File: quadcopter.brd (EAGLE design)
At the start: 137.3 x 137.3 mm, 69 parts, among them J1 AVR_SPI_PRG_6NS, U1 ATMEGA128RFA1, Y2 16MHz

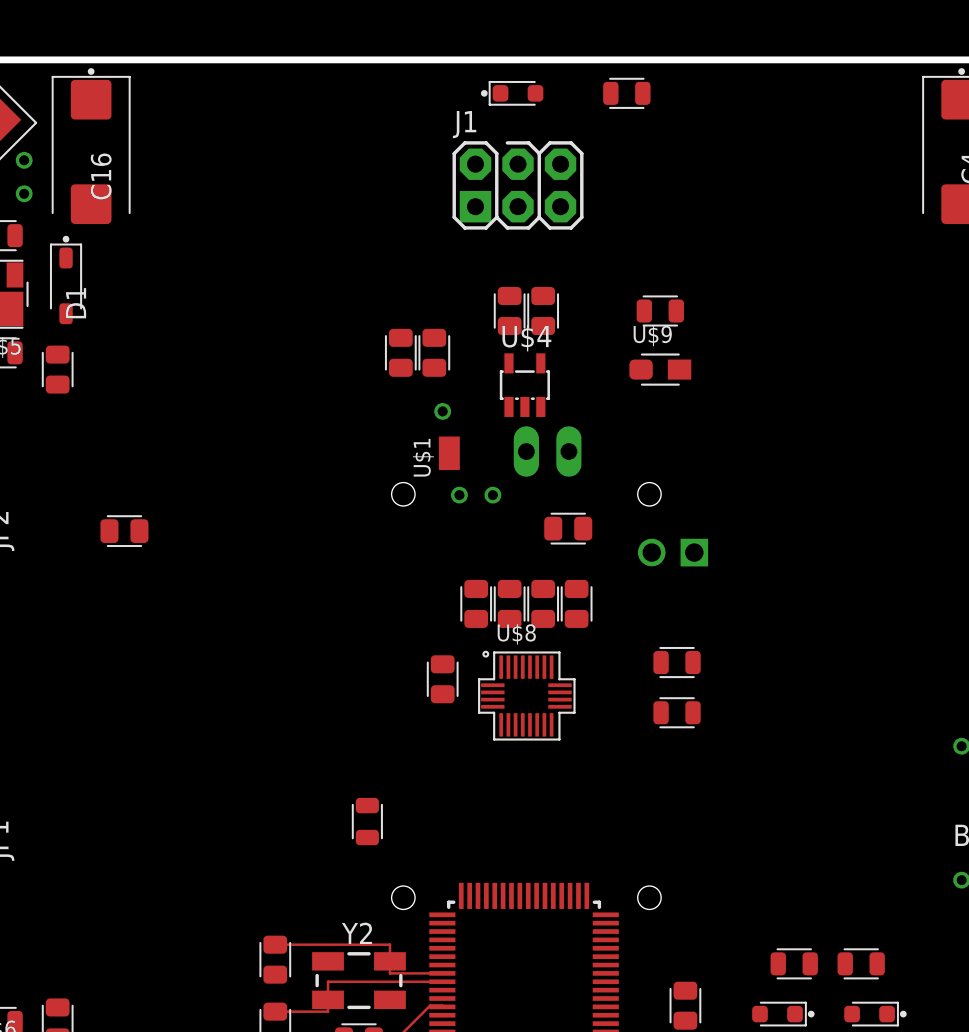
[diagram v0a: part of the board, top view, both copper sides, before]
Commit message: Repositioned battery holder and voltage regulator
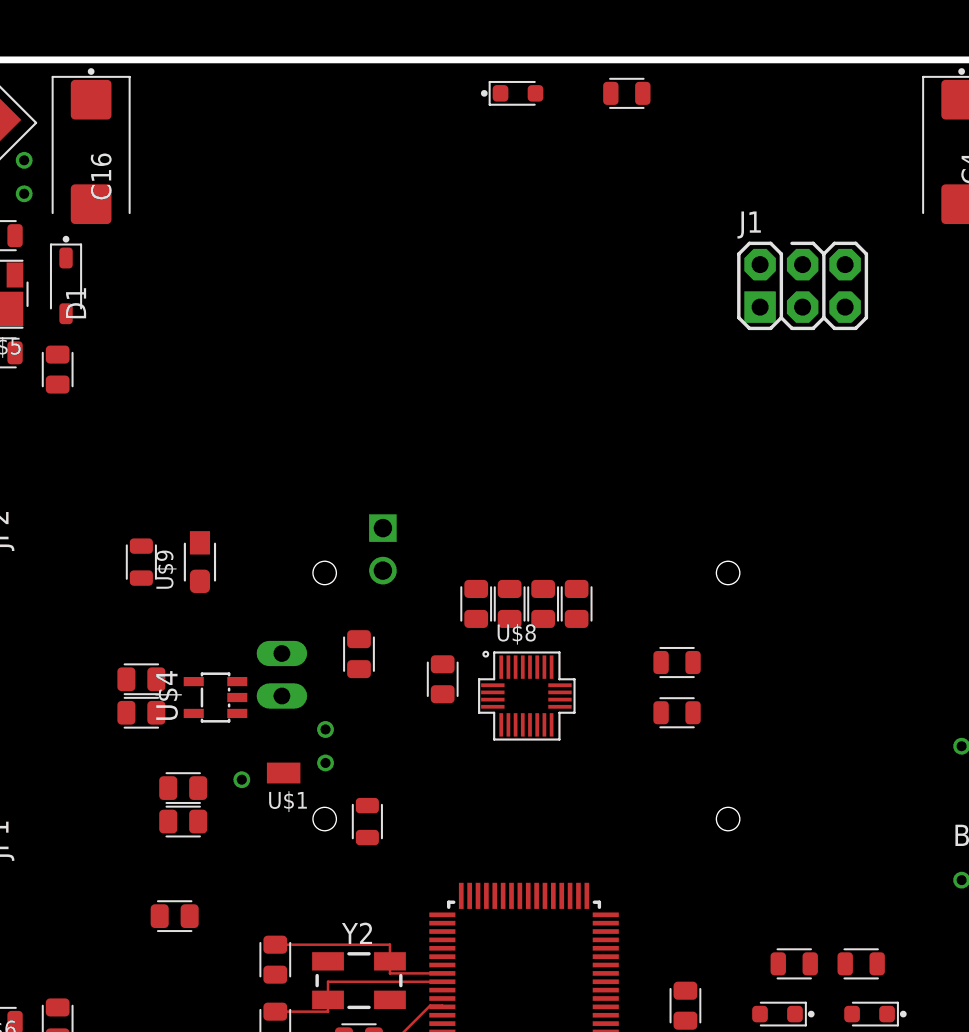
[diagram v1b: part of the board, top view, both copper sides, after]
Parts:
- moved R15 34.4 mm to (15.0, 46.0), turned to 90 degrees
- moved C14 32.6 mm to (15.0, 39.0), turned to 180 degrees
- moved C3 32.6 mm to (15.0, 37.0), turned to 0 degrees
- moved C11 30.9 mm to (17.5, 30.5), turned to 0 degrees
- moved C12 30.0 mm to (17.5, 32.5), turned to 0 degrees
- moved U$9 29.8 mm to (18.5, 46.0), turned to 90 degrees
- moved U$4 26.3 mm to (19.4, 37.9), turned to 90 degrees
- moved C13 23.2 mm to (17.0, 24.9)
- moved U$1 20.8 mm to (24.0, 33.4), turned to 180 degrees
- moved J3 18.7 mm to (29.4, 48.0), turned to 270 degrees
- moved J1 18.0 mm to (54.5, 62.5)
- moved C2 14.6 mm to (28.0, 40.5), turned to 270 degrees
- turned BATT1 to 270 degrees

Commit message: Minor tweaks, added CAM folder
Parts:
- moved D2 7.00 mm to (44.5, 74.0), turned to 180 degrees
- moved R3 6.00 mm to (38.0, 74.0)
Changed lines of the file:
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@@
 <setting verticaltext="up"/>
 </settings>
-<grid distance="1" unitdist="mm" unit="mm" style="lines" multiple="1" display="yes" altdistance="0.025" altunitdist="inch" altunit="inch"/>
+<grid distance="39.3700787" unitdist="mil" unit="mil" style="lines" multiple="1" display="yes" altdistance="0.025" altunitdist="inch" altunit="inch"/>
 <layers>
 <layer number="1" name="Top" color="4" fill="1" visible="yes" active="yes"/>
@@
 </class>
 </classes>
-<designrules name="4pcb-66board">
+<designrules name="batman-4pcb-66board *">
 <description language="de">&lt;b&gt;EAGLE Design Rules&lt;/b&gt;
 &lt;p&gt;
@@
 <attribute name="MPN" value="CRS08(TE85L,Q,M)" x="10.5" y="62.5" size="1.778" layer="27" rot="R270" display="off"/>
 </element>
-<element name="D2" library="quadparts_prebuilt" package="LEDSC125X200X120-2_HS" value="green" x="37.5" y="74">
-<attribute name="DIST" value="Digikey" x="37.5" y="74" size="1.778" layer="27" display="off"/>
-<attribute name="DISTPN" value="160-1179-1-ND" x="37.5" y="74" size="1.778" layer="27" display="off"/>
-<attribute name="MFR" value="Lite-On Inc" x="37.5" y="74" size="1.778" layer="27" display="off"/>
-<attribute name="MPN" value="LTST-C170GKT" x="37.5" y="74" size="1.778" layer="27" display="off"/>
+<element name="D2" library="quadparts_prebuilt" package="LEDSC125X200X120-2_HS" value="green" x="44.5" y="74" rot="R180">
+<attribute name="DIST" value="Digikey" x="44.5" y="74" size="1.778" layer="27" rot="R180" display="off"/>
+<attribute name="DISTPN" value="160-1179-1-ND" x="44.5" y="74" size="1.778" layer="27" rot="R180" display="off"/>
+<attribute name="MFR" value="Lite-On Inc" x="44.5" y="74" size="1.778" layer="27" rot="R180" display="off"/>
+<attribute name="MPN" value="LTST-C170GKT" x="44.5" y="74" size="1.778" layer="27" rot="R180" display="off"/>
 </element>
 <element name="D3" library="quadparts_prebuilt" package="LEDSC125X200X120-2_HS" value="green" x="53" y="19" rot="R180">
@@
 <attribute name="MPN" value="RC0805JR-0710KL" x="69.5" y="64" size="1.778" layer="27" display="off"/>
 </element>
-<element name="R3" library="quadparts_prebuilt" package="RESC2012X60_HS" value="15" x="44" y="74">
-<attribute name="CREATOR" value="Joshua Crook" x="44" y="74" size="1.778" layer="27" display="off"/>
-<attribute name="DIST" value="Digikey" x="44" y="74" size="1.778" layer="27" display="off"/>
-<attribute name="DISTPN" value="311-15ARCT-ND" x="44" y="74" size="1.778" layer="27" display="off"/>
-<attribute name="MFR" value="Yageo" x="44" y="74" size="1.778" layer="27" display="off"/>
-<attribute name="MPN" value="RC0805JR-0715RL" x="44" y="74" size="1.778" layer="27" display="off"/>
-<attribute name="REVIEWER" value="John Wu" x="44" y="74" size="1.778" layer="27" display="off"/>
+<element name="R3" library="quadparts_prebuilt" package="RESC2012X60_HS" value="15" x="38" y="74">
+<attribute name="CREATOR" value="Joshua Crook" x="38" y="74" size="1.778" layer="27" display="off"/>
+<attribute name="DIST" value="Digikey" x="38" y="74" size="1.778" layer="27" display="off"/>
+<attribute name="DISTPN" value="311-15ARCT-ND" x="38" y="74" size="1.778" layer="27" display="off"/>
+<attribute name="MFR" value="Yageo" x="38" y="74" size="1.778" layer="27" display="off"/>
+<attribute name="MPN" value="RC0805JR-0715RL" x="38" y="74" size="1.778" layer="27" display="off"/>
+<attribute name="REVIEWER" value="John Wu" x="38" y="74" size="1.778" layer="27" display="off"/>
 </element>
 <element name="R4" library="quadparts_prebuilt" package="RESC2012X60_HS" value="15" x="54" y="22">
@@
 <via x="31" y="16" extent="1-16" drill="0.6"/>
 <via x="45" y="16" extent="1-16" drill="0.6"/>
-<wire x1="57.04" y1="63.77" x2="36.455" y2="74" width="0" layer="19" extent="1-1"/>
+<wire x1="57.04" y1="63.77" x2="45.545" y2="74" width="0" layer="19" extent="1-1"/>
 <wire x1="39.11" y1="16.299" x2="40" y2="14.5" width="0" layer="19" extent="1-1"/>
 <wire x1="38.61" y1="16.299" x2="39.11" y2="16.299" width="0" layer="19" extent="1-1"/>
@@
 <contactref element="U1" pad="43"/>
 <contactref element="R3" pad="2"/>
-<wire x1="36.61" y1="26.061" x2="44.955" y2="74" width="0" layer="19" extent="1-1"/>
+<wire x1="36.61" y1="26.061" x2="38.955" y2="74" width="0" layer="19" extent="1-1"/>
 </signal>
 <signal name="SCL">
@@
 <contactref element="D2" pad="A"/>
 <contactref element="R3" pad="1"/>
-<wire x1="38.545" y1="74" x2="43.045" y2="74" width="0" layer="19" extent="1-1"/>
+<wire x1="37.045" y1="74" x2="43.455" y2="74" width="0" layer="19" extent="1-1"/>
 </signal>
 <signal name="N$6">

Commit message: Ready to be routed
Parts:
- moved R5 23.7 mm to (49.5, 19.5)
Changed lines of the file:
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@@
 <setting verticaltext="up"/>
 </settings>
-<grid distance="39.3700787" unitdist="mil" unit="mil" style="lines" multiple="1" display="yes" altdistance="0.025" altunitdist="inch" altunit="inch"/>
+<grid distance="1" unitdist="mm" unit="mm" style="lines" multiple="1" display="yes" altdistance="0.025" altunitdist="inch" altunit="inch"/>
 <layers>
 <layer number="1" name="Top" color="4" fill="1" visible="yes" active="yes"/>
@@
 <vertex x="36.5" y="36.75"/>
 </polygon>
-<polygon width="0.4064" layer="40">
-<vertex x="46" y="15"/>
+<polygon width="0.4064" layer="42">
+<vertex x="45.5" y="15"/>
 <vertex x="48" y="15"/>
 <vertex x="48" y="0"/>
 <vertex x="28" y="0"/>
 <vertex x="28" y="15"/>
-<vertex x="30" y="15"/>
-<vertex x="30" y="7"/>
-<vertex x="46" y="7"/>
+<vertex x="30.5" y="15"/>
+<vertex x="30.5" y="7.5"/>
+<vertex x="45.5" y="7.5"/>
 </polygon>
-<polygon width="0.4064" layer="39">
+<polygon width="0.4064" layer="41">
 <vertex x="28" y="15"/>
 <vertex x="28" y="0"/>
 <vertex x="48" y="0"/>
 <vertex x="48" y="15"/>
-<vertex x="46" y="15"/>
-<vertex x="46" y="7"/>
-<vertex x="30" y="7"/>
-<vertex x="30" y="15"/>
+<vertex x="45.5" y="15"/>
+<vertex x="45.5" y="7.5"/>
+<vertex x="30.5" y="7.5"/>
+<vertex x="30.5" y="15"/>
 </polygon>
 <wire x1="-24.55" y1="104.1" x2="-28.05" y2="100.6" width="0.4064" layer="20" curve="-287.803432"/>
@@
 </class>
 </classes>
-<designrules name="batman-4pcb-66board *">
+<designrules name="batman-4pcb-66board">
 <description language="de">&lt;b&gt;EAGLE Design Rules&lt;/b&gt;
 &lt;p&gt;
@@
 <attribute name="REVIEWER" value="John Wu" x="54" y="22" size="1.778" layer="27" display="off"/>
 </element>
-<element name="R5" library="quadparts_prebuilt" package="RESC2012X60_HS" value="10K" x="28.5" y="30.5" rot="R90">
-<attribute name="DIST" value="Digikey" x="28.5" y="30.5" size="1.778" layer="27" rot="R90" display="off"/>
-<attribute name="DISTPN" value="311-10KARCT-ND" x="28.5" y="30.5" size="1.778" layer="27" rot="R90" display="off"/>
-<attribute name="MFR" value="Yageo" x="28.5" y="30.5" size="1.778" layer="27" rot="R90" display="off"/>
-<attribute name="MPN" value="RC0805JR-0710KL" x="28.5" y="30.5" size="1.778" layer="27" rot="R90" display="off"/>
+<element name="R5" library="quadparts_prebuilt" package="RESC2012X60_HS" value="10K" x="49.5" y="19.5" rot="R90">
+<attribute name="DIST" value="Digikey" x="49.5" y="19.5" size="1.778" layer="27" rot="R90" display="off"/>
+<attribute name="DISTPN" value="311-10KARCT-ND" x="49.5" y="19.5" size="1.778" layer="27" rot="R90" display="off"/>
+<attribute name="MFR" value="Yageo" x="49.5" y="19.5" size="1.778" layer="27" rot="R90" display="off"/>
+<attribute name="MPN" value="RC0805JR-0710KL" x="49.5" y="19.5" size="1.778" layer="27" rot="R90" display="off"/>
 </element>
 <element name="R6" library="quadparts_prebuilt" package="RESC2012X60_HS" value="100" x="6.5" y="58.5">
@@
 <wire x1="39" y1="42.605" x2="37" y2="42.605" width="0" layer="19" extent="1-1"/>
 <wire x1="33" y1="38.105" x2="35.995" y2="38.215" width="0" layer="19" extent="1-1"/>
-<wire x1="28.5" y1="31.455" x2="33" y2="38.105" width="0" layer="19" extent="1-1"/>
-<wire x1="36.11" y1="26.061" x2="28.5" y2="31.455" width="0" layer="19" extent="1-1"/>
+<wire x1="36.11" y1="26.061" x2="36.925" y2="36.275" width="0" layer="19" extent="1-1"/>
 <wire x1="32.979" y1="22.43" x2="36.11" y2="26.061" width="0" layer="19" extent="1-1"/>
 <wire x1="32.979" y1="19.93" x2="32.979" y2="22.43" width="0" layer="19" extent="1-1"/>
 <wire x1="41.11" y1="26.061" x2="36.11" y2="26.061" width="0" layer="19" extent="1-1"/>
 <wire x1="42.741" y1="20.43" x2="41.11" y2="26.061" width="0" layer="19" extent="1-1"/>
-<wire x1="18.13" y1="36.96" x2="28.5" y2="31.455" width="0" layer="19" extent="1-1"/>
+<wire x1="49.5" y1="20.455" x2="42.741" y2="20.43" width="0" layer="19" extent="1-1"/>
+<wire x1="18.13" y1="36.96" x2="33" y2="38.105" width="0" layer="19" extent="1-1"/>
 <wire x1="15.895" y1="37" x2="18.13" y2="36.96" width="0" layer="19" extent="1-1"/>
 <wire x1="16.605" y1="32.5" x2="15.895" y2="37" width="0" layer="19" extent="1-1"/>
@@
 <contactref element="C13" pad="2"/>
 <contactref element="J1" pad="5"/>
-<wire x1="28.5" y1="29.545" x2="57.04" y2="61.23" width="0" layer="19" extent="1-1"/>
-<wire x1="17.885" y1="24.85" x2="28.5" y2="29.545" width="0" layer="19" extent="1-1"/>
-<wire x1="39.61" y1="16.299" x2="28.5" y2="29.545" width="0" layer="19" extent="1-1"/>
+<wire x1="49.5" y1="18.545" x2="57.04" y2="61.23" width="0" layer="19" extent="1-1"/>
+<wire x1="39.61" y1="16.299" x2="49.5" y2="18.545" width="0" layer="19" extent="1-1"/>
+<wire x1="17.885" y1="24.85" x2="39.61" y2="16.299" width="0" layer="19" extent="1-1"/>
 </signal>
 <signal name="N$4">
